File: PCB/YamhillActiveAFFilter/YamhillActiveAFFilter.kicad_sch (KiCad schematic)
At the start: 30 parts, among them J1 Input, J2 +5V, J3 Output, U1 TL974

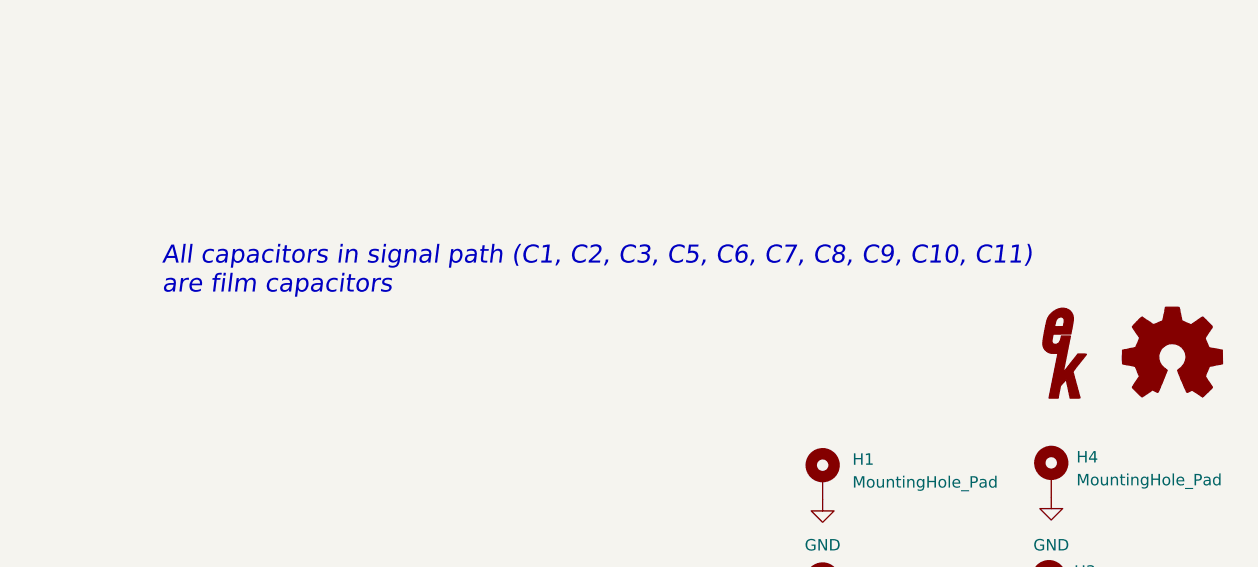
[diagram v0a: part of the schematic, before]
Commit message: AF Filter, Protoboard modules added
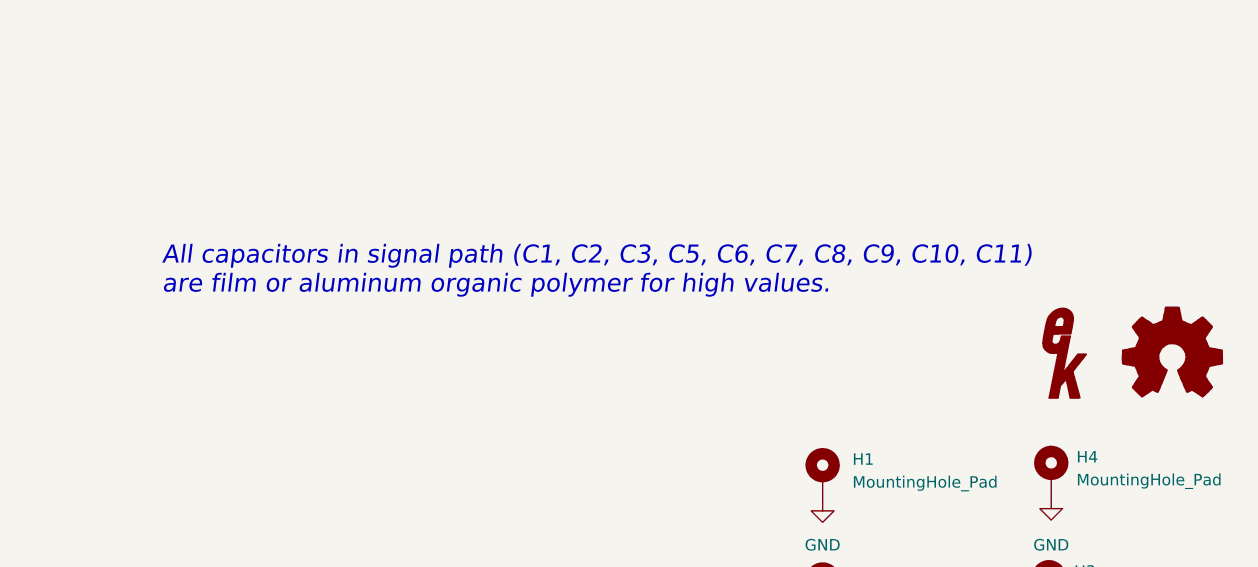
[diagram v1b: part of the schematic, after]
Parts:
- C10, C8: footprint Capacitor_THT:C_Rect_L7.0mm_W2.5mm_P5.00mm -> Capacitor_THT:CP_Radial_D8.0mm_P3.50mm
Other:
- note added: "All capacitors in signal path (C1, C2, C3, C5, C6, C7, C8, C9, C10, C11) are film or aluminum organic polymer for high values."
- note removed: "All capacitors in signal path (C1, C2, C3, C5, C6, C7, C8, C9, C10, C11) are film capacitors"
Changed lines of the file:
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@@
     (effects (font (size 2 2) (thickness 0.254) bold) (justify left bottom))
   )
-  (text "All capacitors in signal path (C1, C2, C3, C5, C6, C7, C8, C9, C10, C11)\nare film capacitors"
+  (text "All capacitors in signal path (C1, C2, C3, C5, C6, C7, C8, C9, C10, C11)\nare film or aluminum organic polymer for high values."
     (at 38.1 161.29 0)
     (effects (font (size 2 2) italic) (justify left bottom))
@@
       (effects (font (size 1.27 1.27)) (justify left) hide)
     )
-    (property "Footprint" "Capacitor_THT:C_Rect_L7.0mm_W2.5mm_P5.00mm" (at 176.657 63.5 0)
+    (property "Footprint" "Capacitor_THT:CP_Radial_D8.0mm_P3.50mm" (at 176.657 63.5 0)
       (effects (font (size 1.27 1.27)) hide)
     )
@@
       (effects (font (size 1.27 1.27)) (justify left) hide)
     )
-    (property "Footprint" "Capacitor_THT:C_Rect_L7.0mm_W2.5mm_P5.00mm" (at 227.457 63.5 0)
-      (effects (font (size 1.27 1.27)) hide)
-    )
+    (property "Footprint" "Capacitor_THT:CP_Radial_D8.0mm_P3.50mm" (at 227.457 63.5 0)
+      (effects (font (size 1.27 1.27)) hide)
+    )

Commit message: Front Panel Rev B revisions
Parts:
- removed U1: TL974, Package_DIP:DIP-14_W7.62mm_LongPads, symbol EtherkitKicadLibrary:OPAMP-QUAD
- added U1, U2: TLV9362, EtherkitKicadLibrary:DIP-8_SOIC-8_Combo, symbol EtherkitKicadLibrary:OPAMP-DUAL
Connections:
- net GND: now also U1.4 (V-), U2.4 (V-)
- net at C6.2, R8.1: now also U1.6 (-), U1.7
- net at C3.2, R6.1: now also U1.1, U1.2 (-)
- net at C2.1, R4.2: now also U1.3 (+)
- net at C4.1, R1.1, R5.2: now also U1.8 (V+), U2.8 (V+)
- net at C10.2, C11.1: now also U2.6 (-), U2.7
- net at C9.1, R11.2: now also U2.5 (+)
- net at C5.1, R7.2: now also U1.5 (+)
- net at C8.2, R10.1: now also U2.1, U2.2 (-)
- net at C7.1, R9.2: now also U2.3 (+)
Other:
- moved on the sheet: C8
